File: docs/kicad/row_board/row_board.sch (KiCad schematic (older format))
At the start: 19 parts, among them J1 Conn_01x06, J2 Conn_01x06, SW1 SW1, SW2 SW1, SW3 SW1, SW4 SW1, SW5 SW1, U1 74HC595

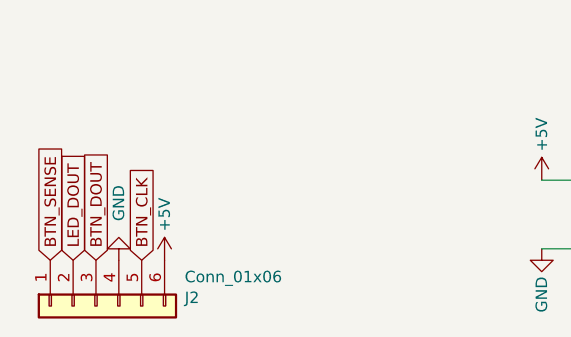
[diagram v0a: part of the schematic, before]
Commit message: new row board design (with chip at left end)
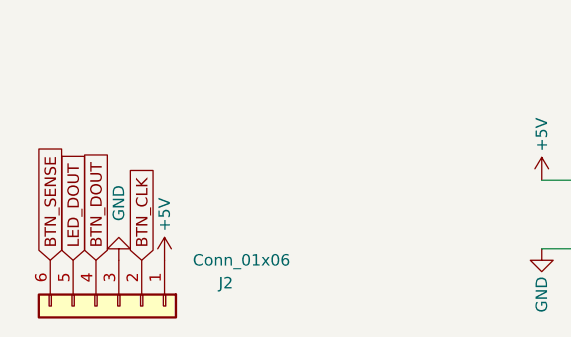
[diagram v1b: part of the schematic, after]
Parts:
- J1, J2: footprint 0_my_footprints:my6Pin-08mm -> 0_my_footprints:invRightAngleJSTx06
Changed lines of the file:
@@
 F 0 "J1" V 914 412 50  0000 R CNN
 F 1 "Conn_01x06" V 823 412 50  0000 R CNN
-F 2 "0_my_footprints:my6Pin-08mm" H 950 800 50  0001 C CNN
+F 2 "0_my_footprints:invRightAngleJSTx06" H 950 800 50  0001 C CNN
 F 3 "~" H 950 800 50  0001 C CNN
 	1    950  800
@@
 L Connector_Generic:Conn_01x06 J2
 U 1 1 6608525E
-P 1000 3600
-F 0 "J2" V 964 3212 50  0000 R CNN
-F 1 "Conn_01x06" V 873 3212 50  0000 R CNN
-F 2 "0_my_footprints:my6Pin-08mm" H 1000 3600 50  0001 C CNN
-F 3 "~" H 1000 3600 50  0001 C CNN
-	1    1000 3600
-	0    -1   1    0
-$EndComp
-$Comp
+P 1100 3600
+F 0 "J2" V 1000 4100 50  0000 R CNN
+F 1 "Conn_01x06" V 900 4350 50  0000 R CNN
+F 2 "0_my_footprints:invRightAngleJSTx06" H 1100 3600 50  0001 C CNN
+F 3 "~" H 1100 3600 50  0001 C CNN
+	1    1100 3600
+	0    1    1    0
+$EndComp
+$Comp

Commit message: kicad changes to support actual Fusion 360 TE3 design efforts - created rotary board PCB
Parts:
- J2: footprint 0_my_footprints:invRightAngleJSTx06 -> 0_my_footprints:my6Pin-08mm
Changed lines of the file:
@@
 F 0 "J2" V 1000 4100 50  0000 R CNN
 F 1 "Conn_01x06" V 900 4350 50  0000 R CNN
-F 2 "0_my_footprints:invRightAngleJSTx06" H 1100 3600 50  0001 C CNN
+F 2 "0_my_footprints:my6Pin-08mm" H 1100 3600 50  0001 C CNN
 F 3 "~" H 1100 3600 50  0001 C CNN
 	1    1100 3600
